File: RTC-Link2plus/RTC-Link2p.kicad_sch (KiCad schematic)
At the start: 16 parts, among them CN1 EDGE_CON_02x12, J1 Conn_02x07_Odd_Even, J2 Flyout1, J3 Flyout2, J4 Conn_02x07_Top_Bottom, P1 c64cartedge, U1 MC68A21, U2 74LS30, U3 74LS00, U5 27C512PLCC

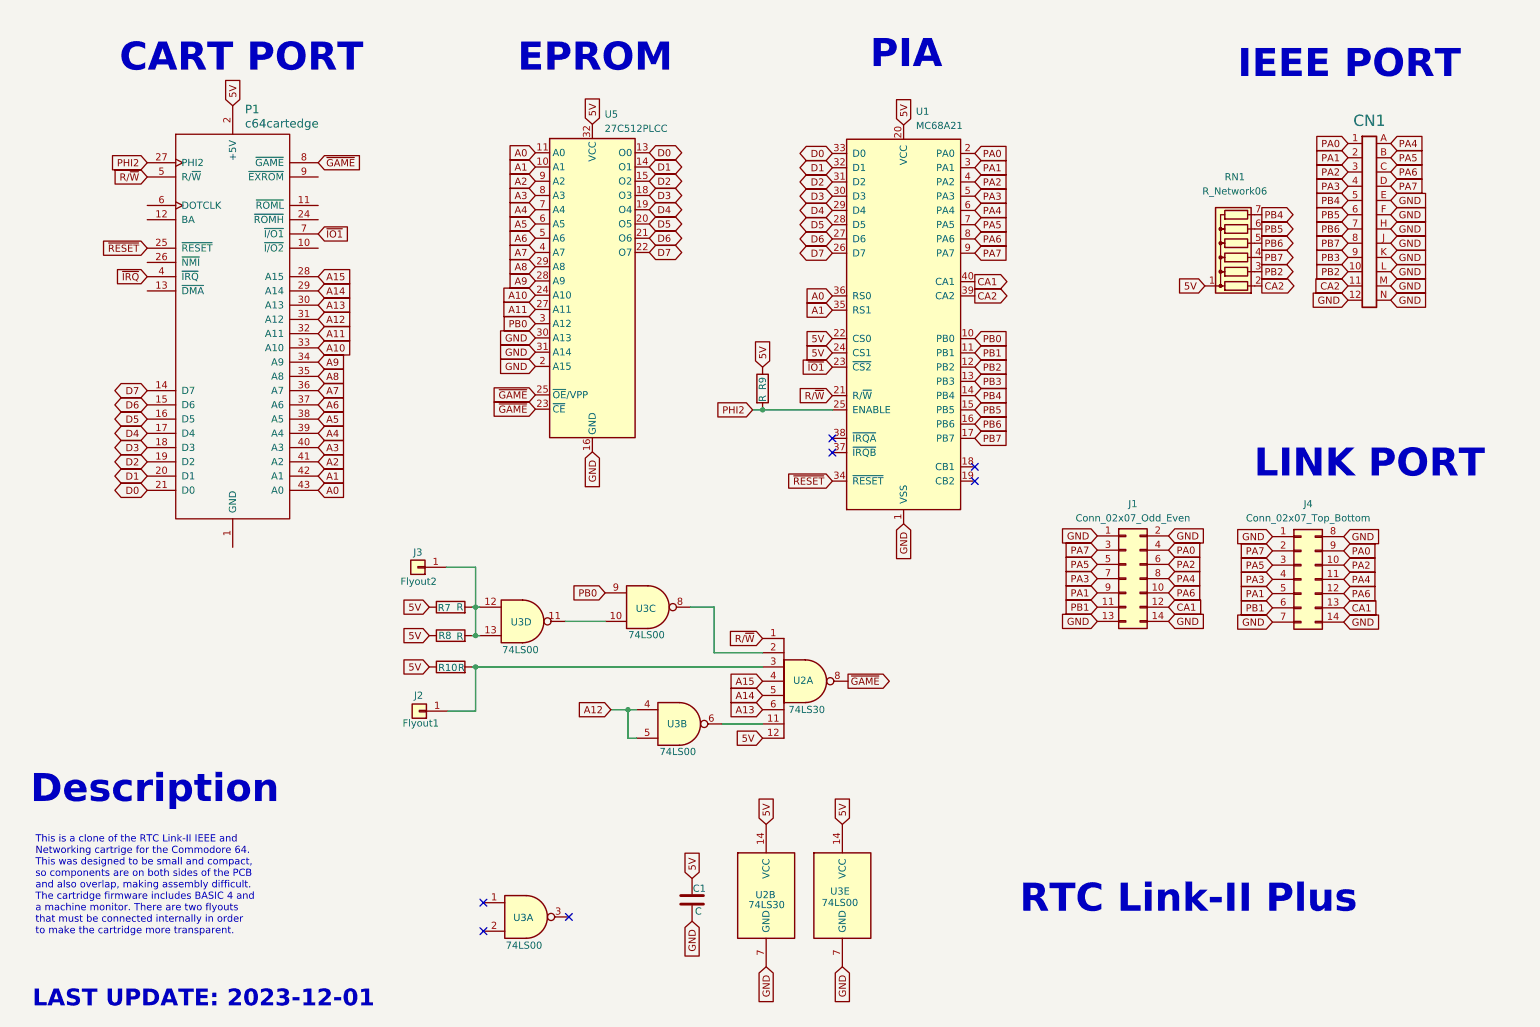
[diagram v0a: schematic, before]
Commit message: Update to Kicad 9. Add Gerbers, component values, iBom
Update files to Kicad 9 format. Add Gerbers. Add more component values. Generate interactive BOM.  Boards have been made but not tested. Use at own risk!
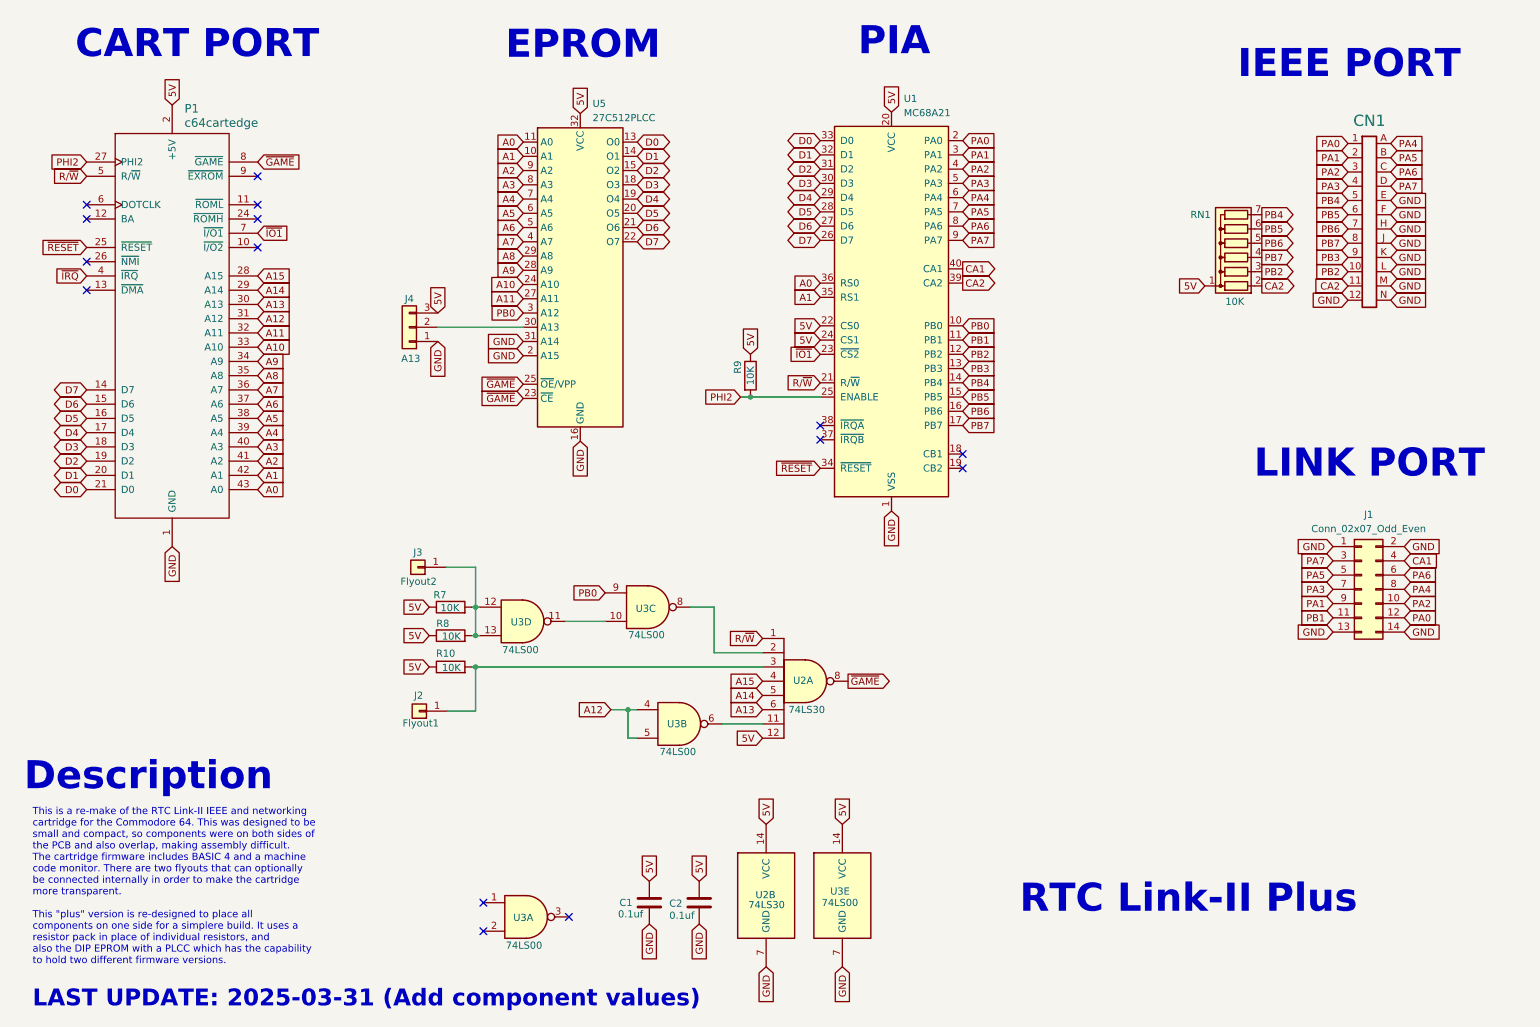
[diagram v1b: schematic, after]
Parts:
- removed J4: Conn_02x07_Top_Bottom, Connector_PinHeader_2.54mm:PinHeader_2x07_P2.54mm_Vertical, symbol Connector_Generic:Conn_02x07_Top_Bottom
- added C2: 0.1uf, Capacitor_THT:C_Disc_D3.0mm_W1.6mm_P2.50mm, symbol Device:C
- added J4: A13, Connector_PinHeader_2.54mm:PinHeader_1x03_P2.54mm_Vertical, symbol Connector_Generic:Conn_01x03
- C1: value C -> 0.1uf; footprint Connector_PinHeader_2.54mm:PinHeader_2x07_P2.54mm_Vertical -> Capacitor_THT:C_Disc_D3.0mm_W1.6mm_P2.50mm
- R10, R7, R8, R9: value R -> 10K
- RN1: value R_Network06 -> 10K
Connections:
- net +5V: now also C2.1, J4.3 (Pin_3)
- net CA1: now also J1.4 (Pin_4); no longer J1.12 (Pin_12)
- net GND: now also C2.2, J4.1 (Pin_1); no longer U5.30 (A13)
- net PA0: now also J1.12 (Pin_12); no longer J1.4 (Pin_4)
- net PA2: now also J1.10 (Pin_10); no longer J1.6 (Pin_6)
- net PA6: now also J1.6 (Pin_6); no longer J1.10 (Pin_10)
- new net: J4.2 (Pin_2), U5.30 (A13)
- no-connect marks 7 -> 15
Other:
- note added: "LAST UPDATE: 2025-03-31 (Add component values)"
- note added: "This is a re-make of the RTC Link-II IEEE and networking cartridge for the Commodore 64. This was designed to be small and compact, so components were on both sides of the PCB and also overlap, making assembly difficult. The cartridge firmware includes BASIC 4 and a machine code monitor. There are two flyouts that can optionally be connected internally in order to make the cartridge more transpar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"
- note removed: "LAST UPDATE: 2023-12-01"
- note removed: "This is a clone of the RTC Link-II IEEE and Networking cartrige for the Commodore 64. This was designed to be small and compact, so components are on both sides of the PCB and also overlap, making assembly difficult. The cartridge firmware includes BASIC 4 and a machine monitor. There are two flyouts that must be connected internally in order to make the cartridge more transparent."
- moved on the sheet: C1, J1, P1, R9, U1, U5
